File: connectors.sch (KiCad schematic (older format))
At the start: 43 parts, among them J11 20021121-00010C4LF, J12 70543-0001, J13 70543-0001, J14 70543-0001, J15 70543-0001, J16 70543-0001, J17 70543-0001, J18 70543-0001, J19 70543-0001, J20 70543-0003, J21 70543-0002, J22 70543-0002, J23 70543-0002, J24 Conn_02x20_Odd_Even

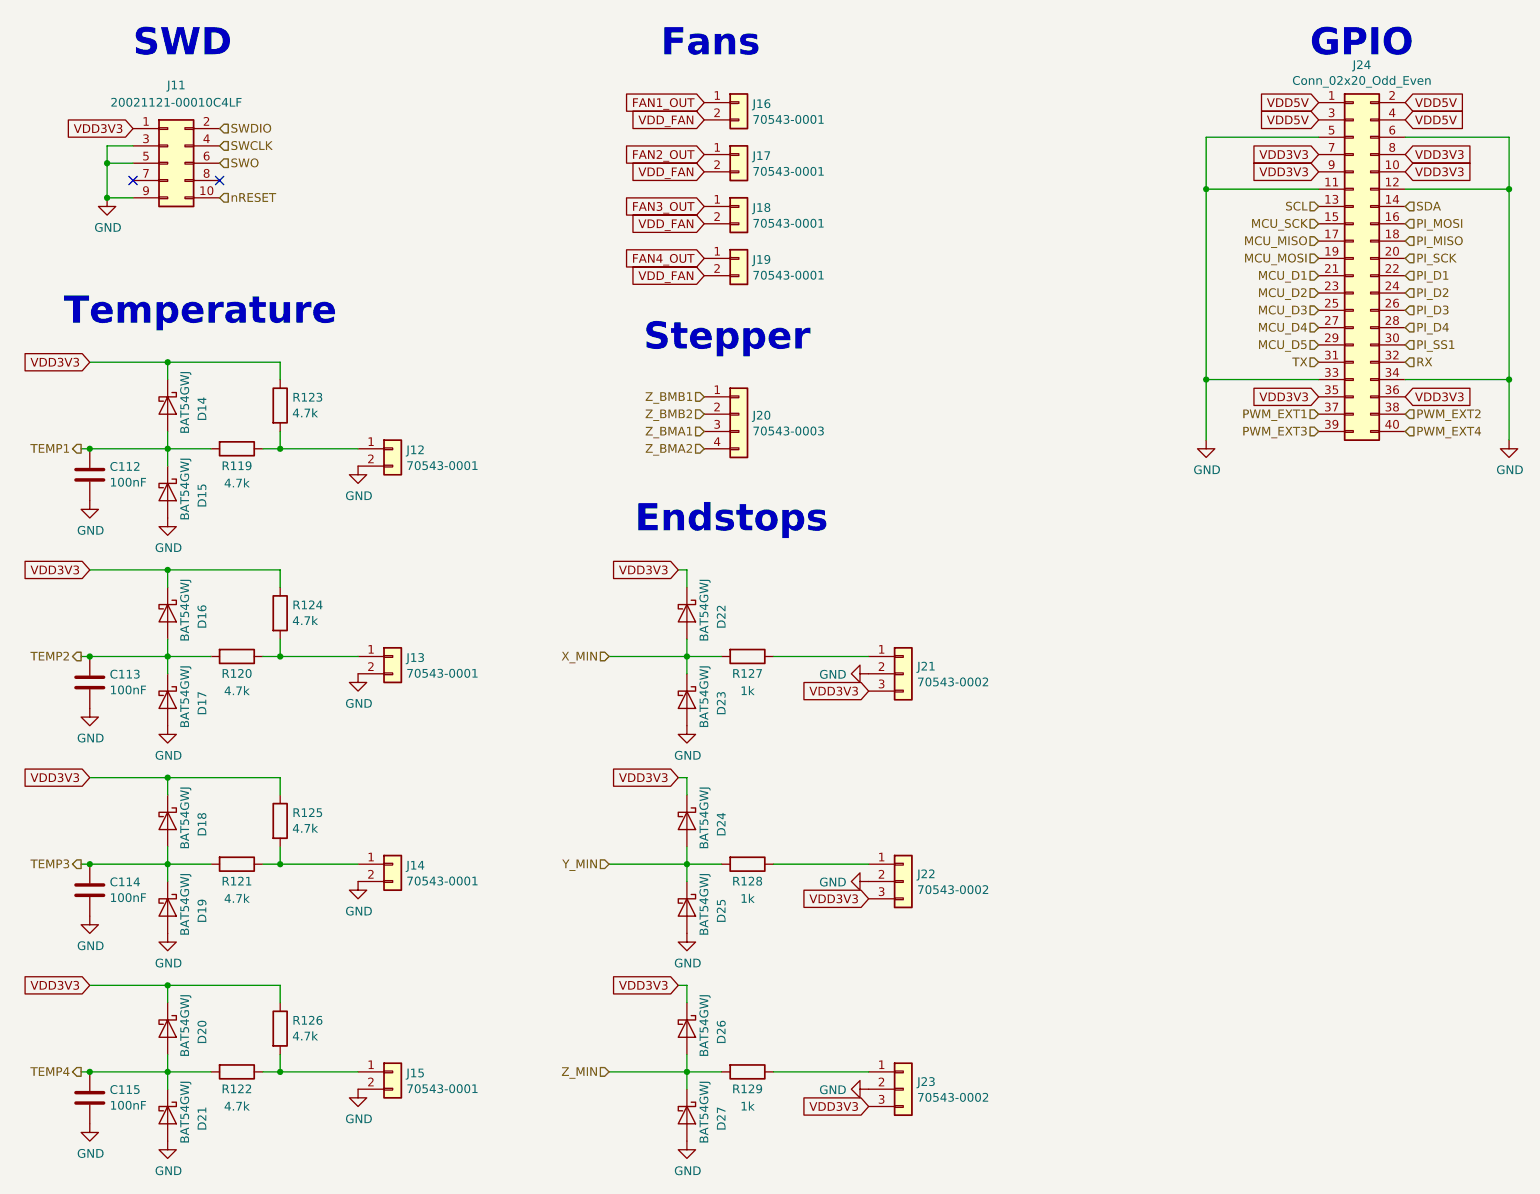
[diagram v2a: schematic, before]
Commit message: Add PU for SD_DETECT_PIN
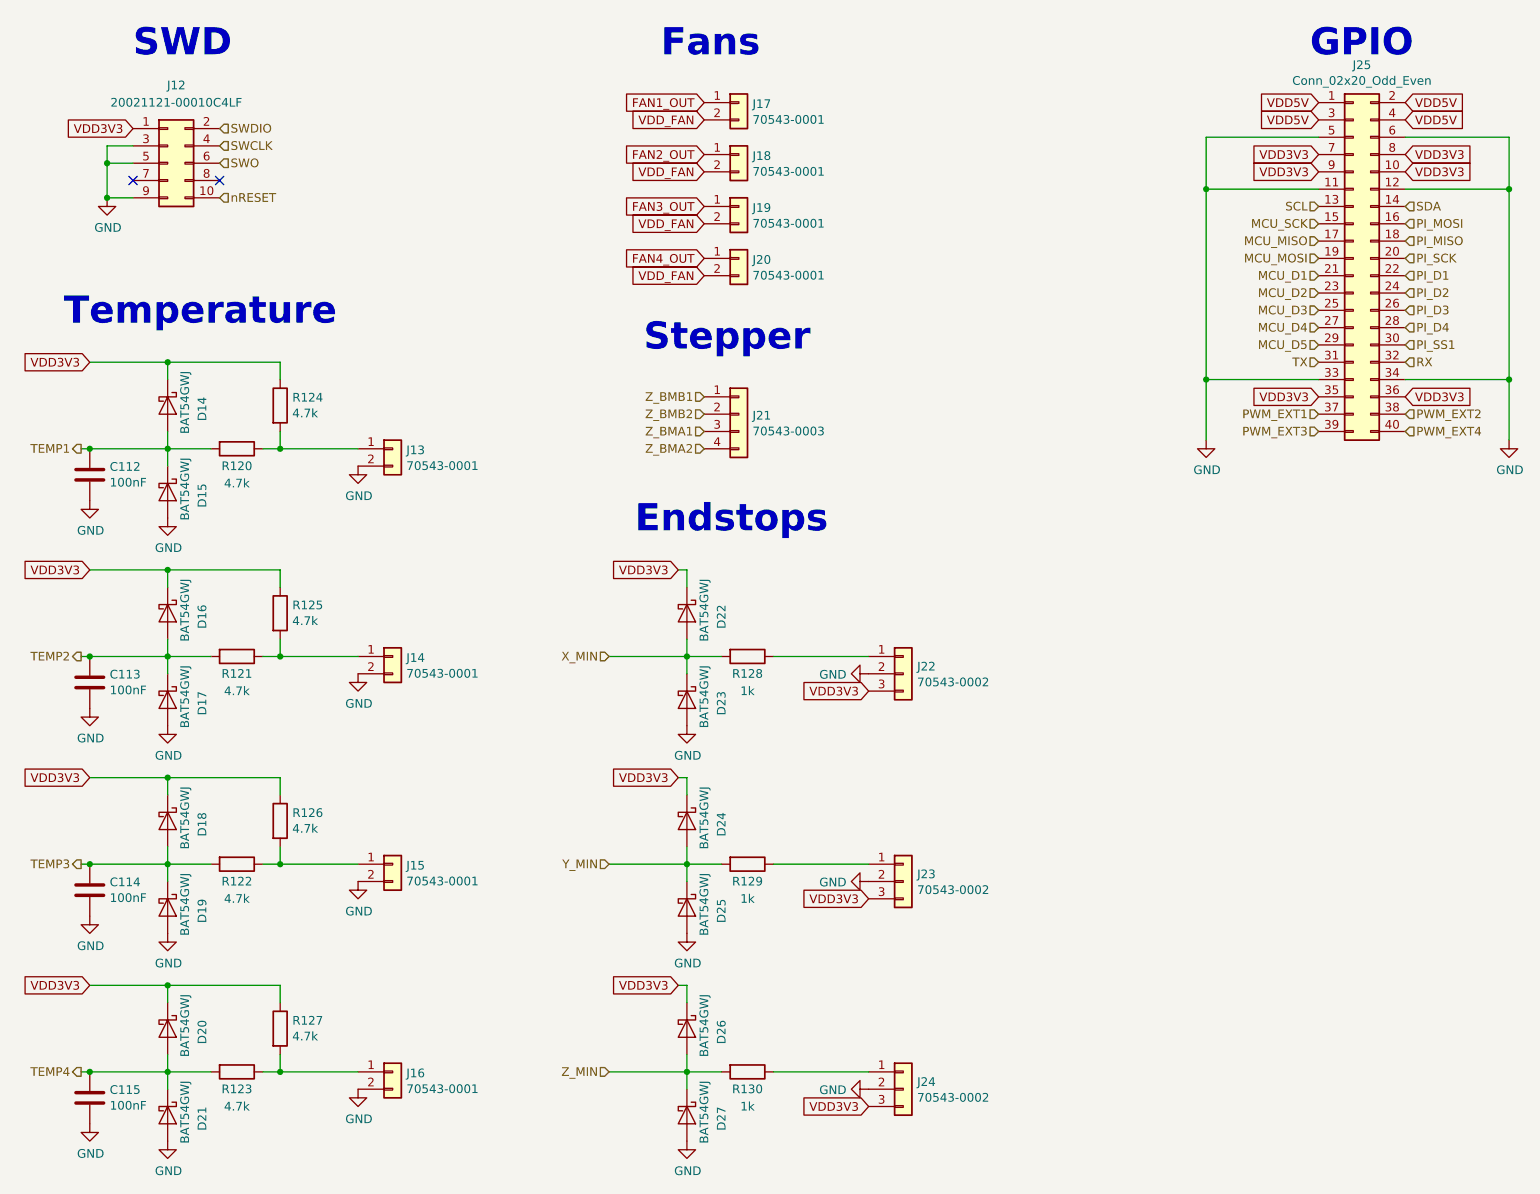
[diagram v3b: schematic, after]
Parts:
- renumbered J11 to J12, J12 to J13, J13 to J14, J14 to J15, J15 to J16, J16 to J17, J17 to J18, J18 to J19, J19 to J20, J20 to J21, J21 to J22, J22 to J23, J23 to J24, J24 to J25, R119 to R120, R120 to R121, R121 to R122, R122 to R123, R123 to R124, R124 to R125, R125 to R126, R126 to R127, R127 to R128, R128 to R129, R129 to R130
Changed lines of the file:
@@
 TEMP1
 $Comp
-L Device:R R119
+L Device:R R120
 U 1 1 5B1719A1
 P 1900 3300
-F 0 "R119" V 2000 3300 50  0000 C CNN
+F 0 "R120" V 2000 3300 50  0000 C CNN
 F 1 "4.7k" V 2100 3300 50  0000 C CNN
 F 2 "Resistor_SMD:R_0603_1608Metric" V 1830 3300 50  0001 C CNN
@@
 $EndComp
 $Comp
-L Device:R R123
+L Device:R R124
 U 1 1 5B1719A8
 P 2150 3050
-F 0 "R123" H 2220 3096 50  0000 L CNN
+F 0 "R124" H 2220 3096 50  0000 L CNN
 F 1 "4.7k" H 2220 3005 50  0000 L CNN
 F 2 "Resistor_SMD:R_0603_1608Metric" V 2080 3050 50  0001 C CNN
@@
 	2150 3300 2150 3200
 $Comp
-L Connector_Generic:Conn_01x02 J12
+L Connector_Generic:Conn_01x02 J13
 U 1 1 5B1719C1
 P 2800 3300
-F 0 "J12" H 2879 3292 50  0000 L CNN
+F 0 "J13" H 2879 3292 50  0000 L CNN
 F 1 "70543-0001" H 2879 3201 50  0000 L CNN
 F 2 "heteromycin:70543-0001" H 2800 3300 50  0001 C CNN
@@
 $EndComp
 $Comp
-L Connector_Generic:Conn_02x05_Odd_Even J11
+L Connector_Generic:Conn_02x05_Odd_Even J12
 U 1 1 5B17C4BC
 P 1500 1650
-F 0 "J11" H 1550 2100 50  0000 C CNN
+F 0 "J12" H 1550 2100 50  0000 C CNN
 F 1 "20021121-00010C4LF" H 1550 2000 50  0000 C CNN
 F 2 "Connector_PinHeader_1.27mm:PinHeader_2x05_P1.27mm_Vertical_SMD" H 1500 1650 50  0001 C CNN
@@
 NoConn ~ 1800 1750
 $Comp
-L Connector_Generic:Conn_01x04 J20
+L Connector_Generic:Conn_01x04 J21
 U 1 1 5AFD917C
 P 4800 3100
-F 0 "J20" H 4879 3092 50  0000 L CNN
+F 0 "J21" H 4879 3092 50  0000 L CNN
 F 1 "70543-0003" H 4879 3001 50  0000 L CNN
 F 2 "heteromycin:70543-0003" H 4800 3100 50  0001 C CNN
@@
 VDD_FAN
 $Comp
-L Device:R R127
+L Device:R R128
 U 1 1 5B40FD8A
 P 4850 4500
-F 0 "R127" V 4950 4500 50  0000 C CNN
+F 0 "R128" V 4950 4500 50  0000 C CNN
 F 1 "1k" V 5050 4500 50  0000 C CNN
 F 2 "Resistor_SMD:R_0603_1608Metric" V 4780 4500 50  0001 C CNN
@@
 	4500 4500 4700 4500
 $Comp
-L Device:R R128
+L Device:R R129
 U 1 1 5B453619
 P 4850 5700
-F 0 "R128" V 4950 5700 50  0000 C CNN
+F 0 "R129" V 4950 5700 50  0000 C CNN
 F 1 "1k" V 5050 5700 50  0000 C CNN
 F 2 "Resistor_SMD:R_0603_1608Metric" V 4780 5700 50  0001 C CNN
@@
 	4500 5700 4700 5700
 $Comp
-L Device:R R129
+L Device:R R130
 U 1 1 5B45771E
 P 4850 6900
-F 0 "R129" V 4950 6900 50  0000 C CNN
+F 0 "R130" V 4950 6900 50  0000 C CNN
 F 1 "1k" V 5050 6900 50  0000 C CNN
 F 2 "Resistor_SMD:R_0603_1608Metric" V 4780 6900 50  0001 C CNN
@@
 Connection ~ 2150 3300
 $Comp
-L Device:R R120
+L Device:R R121
 U 1 1 5B5657F4
 P 1900 4500
-F 0 "R120" V 2000 4500 50  0000 C CNN
+F 0 "R121" V 2000 4500 50  0000 C CNN
 F 1 "4.7k" V 2100 4500 50  0000 C CNN
 F 2 "Resistor_SMD:R_0603_1608Metric" V 1830 4500 50  0001 C CNN
@@
 $EndComp
 $Comp
-L Device:R R124
+L Device:R R125
 U 1 1 5B5657FB
 P 2150 4250
-F 0 "R124" H 2220 4296 50  0000 L CNN
+F 0 "R125" H 2220 4296 50  0000 L CNN
 F 1 "4.7k" H 2220 4205 50  0000 L CNN
 F 2 "Resistor_SMD:R_0603_1608Metric" V 2080 4250 50  0001 C CNN
@@
 Connection ~ 2150 4500
 $Comp
-L Device:R R121
+L Device:R R122
 U 1 1 5B57C5BA
 P 1900 5700
-F 0 "R121" V 2000 5700 50  0000 C CNN
+F 0 "R122" V 2000 5700 50  0000 C CNN
 F 1 "4.7k" V 2100 5700 50  0000 C CNN
 F 2 "Resistor_SMD:R_0603_1608Metric" V 1830 5700 50  0001 C CNN
@@
 $EndComp
 $Comp
-L Device:R R125
+L Device:R R126
 U 1 1 5B57C5C1
 P 2150 5450
-F 0 "R125" H 2220 5496 50  0000 L CNN
+F 0 "R126" H 2220 5496 50  0000 L CNN
 F 1 "4.7k" H 2220 5405 50  0000 L CNN
 F 2 "Resistor_SMD:R_0603_1608Metric" V 2080 5450 50  0001 C CNN
@@
 $EndComp
 $Comp
-L Device:R R122
+L Device:R R123
 U 1 1 5BC983A7
 P 1900 6900
-F 0 "R122" V 2000 6900 50  0000 C CNN
+F 0 "R123" V 2000 6900 50  0000 C CNN
 F 1 "4.7k" V 2100 6900 50  0000 C CNN
 F 2 "Resistor_SMD:R_0603_1608Metric" V 1830 6900 50  0001 C CNN
@@
 $EndComp
 $Comp
-L Device:R R126
+L Device:R R127
 U 1 1 5BC983AE
 P 2150 6650
-F 0 "R126" H 2220 6696 50  0000 L CNN
+F 0 "R127" H 2220 6696 50  0000 L CNN
 F 1 "4.7k" H 2220 6605 50  0000 L CNN
 F 2 "Resistor_SMD:R_0603_1608Metric" V 2080 6650 50  0001 C CNN
@@
 	2150 6900 2600 6900
 $Comp
-L Connector_Generic:Conn_01x02 J16
+L Connector_Generic:Conn_01x02 J17
 U 1 1 5BCF44AA
 P 4800 1300
-F 0 "J16" H 4879 1292 50  0000 L CNN
+F 0 "J17" H 4879 1292 50  0000 L CNN
 F 1 "70543-0001" H 4879 1201 50  0000 L CNN
 F 2 "heteromycin:70543-0001" H 4800 1300 50  0001 C CNN
@@
 GPIO
 $Comp
-L Connector_Generic:Conn_02x20_Odd_Even J24
+L Connector_Generic:Conn_02x20_Odd_Even J25
 U 1 1 5BD1EAFC
 P 8350 2200
-F 0 "J24" H 8400 3317 50  0000 C CNN
+F 0 "J25" H 8400 3317 50  0000 C CNN
 F 1 "Conn_02x20_Odd_Even" H 8400 3226 50  0000 C CNN
 F 2 "Connector_PinHeader_2.54mm:PinHeader_2x20_P2.54mm_Vertical_SMD" H 8350 2200 50  0001 C CNN
@@
 $EndComp
 $Comp
-L Connector_Generic:Conn_01x02 J17
+L Connector_Generic:Conn_01x02 J18
 U 1 1 5BC6B4B4
 P 4800 1600
-F 0 "J17" H 4879 1592 50  0000 L CNN
+F 0 "J18" H 4879 1592 50  0000 L CNN
 F 1 "70543-0001" H 4879 1501 50  0000 L CNN
 F 2 "heteromycin:70543-0001" H 4800 1600 50  0001 C CNN
@@
 $EndComp
 $Comp
-L Connector_Generic:Conn_01x02 J18
+L Connector_Generic:Conn_01x02 J19
 U 1 1 5BC6CFF2
 P 4800 1900
-F 0 "J18" H 4879 1892 50  0000 L CNN
+F 0 "J19" H 4879 1892 50  0000 L CNN
 F 1 "70543-0001" H 4879 1801 50  0000 L CNN
 F 2 "heteromycin:70543-0001" H 4800 1900 50  0001 C CNN
@@
 $EndComp
 $Comp
-L Connector_Generic:Conn_01x02 J19
+L Connector_Generic:Conn_01x02 J20
 U 1 1 5BC6EB34
 P 4800 2200
-F 0 "J19" H 4879 2192 50  0000 L CNN
+F 0 "J20" H 4879 2192 50  0000 L CNN
 F 1 "70543-0001" H 4879 2101 50  0000 L CNN
 F 2 "heteromycin:70543-0001" H 4800 2200 50  0001 C CNN
@@
 $EndComp
 $Comp
-L Connector_Generic:Conn_01x02 J13
+L Connector_Generic:Conn_01x02 J14
 U 1 1 5BC787B3
 P 2800 4500
-F 0 "J13" H 2879 4492 50  0000 L CNN
+F 0 "J14" H 2879 4492 50  0000 L CNN
 F 1 "70543-0001" H 2879 4401 50  0000 L CNN
 F 2 "heteromycin:70543-0001" H 2800 4500 50  0001 C CNN
@@
 $EndComp
 $Comp
-L Connector_Generic:Conn_01x02 J14
+L Connector_Generic:Conn_01x02 J15
 U 1 1 5BC7A30D
 P 2800 5700
-F 0 "J14" H 2879 5692 50  0000 L CNN
+F 0 "J15" H 2879 5692 50  0000 L CNN
 F 1 "70543-0001" H 2879 5601 50  0000 L CNN
 F 2 "heteromycin:70543-0001" H 2800 5700 50  0001 C CNN
@@
 $EndComp
 $Comp
-L Connector_Generic:Conn_01x02 J15
+L Connector_Generic:Conn_01x02 J16
 U 1 1 5BC7BE61
 P 2800 6900
-F 0 "J15" H 2879 6892 50  0000 L CNN
+F 0 "J16" H 2879 6892 50  0000 L CNN
 F 1 "70543-0001" H 2879 6801 50  0000 L CNN
 F 2 "heteromycin:70543-0001" H 2800 6900 50  0001 C CNN
@@
 FAN4_OUT
 $Comp
-L Connector_Generic:Conn_01x03 J21
+L Connector_Generic:Conn_01x03 J22
 U 1 1 5BCA3C01
 P 5750 4600
-F 0 "J21" H 5830 4642 50  0000 L CNN
+F 0 "J22" H 5830 4642 50  0000 L CNN
 F 1 "70543-0002" H 5830 4551 50  0000 L CNN
 F 2 "heteromycin:70543-0002" H 5750 4600 50  0001 C CNN
@@
 $EndComp
 $Comp
-L Connector_Generic:Conn_01x03 J22
+L Connector_Generic:Conn_01x03 J23
 U 1 1 5BCAFD14
 P 5750 5800
-F 0 "J22" H 5830 5842 50  0000 L CNN
+F 0 "J23" H 5830 5842 50  0000 L CNN
 F 1 "70543-0002" H 5830 5751 50  0000 L CNN
 F 2 "heteromycin:70543-0002" H 5750 5800 50  0001 C CNN
@@
 $EndComp
 $Comp
-L Connector_Generic:Conn_01x03 J23
+L Connector_Generic:Conn_01x03 J24
 U 1 1 5BCB490A
 P 5750 7000
-F 0 "J23" H 5830 7042 50  0000 L CNN
+F 0 "J24" H 5830 7042 50  0000 L CNN
 F 1 "70543-0002" H 5830 6951 50  0000 L CNN
 F 2 "heteromycin:70543-0002" H 5750 7000 50  0001 C CNN

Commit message: Further Improved Readability - Rotated labels
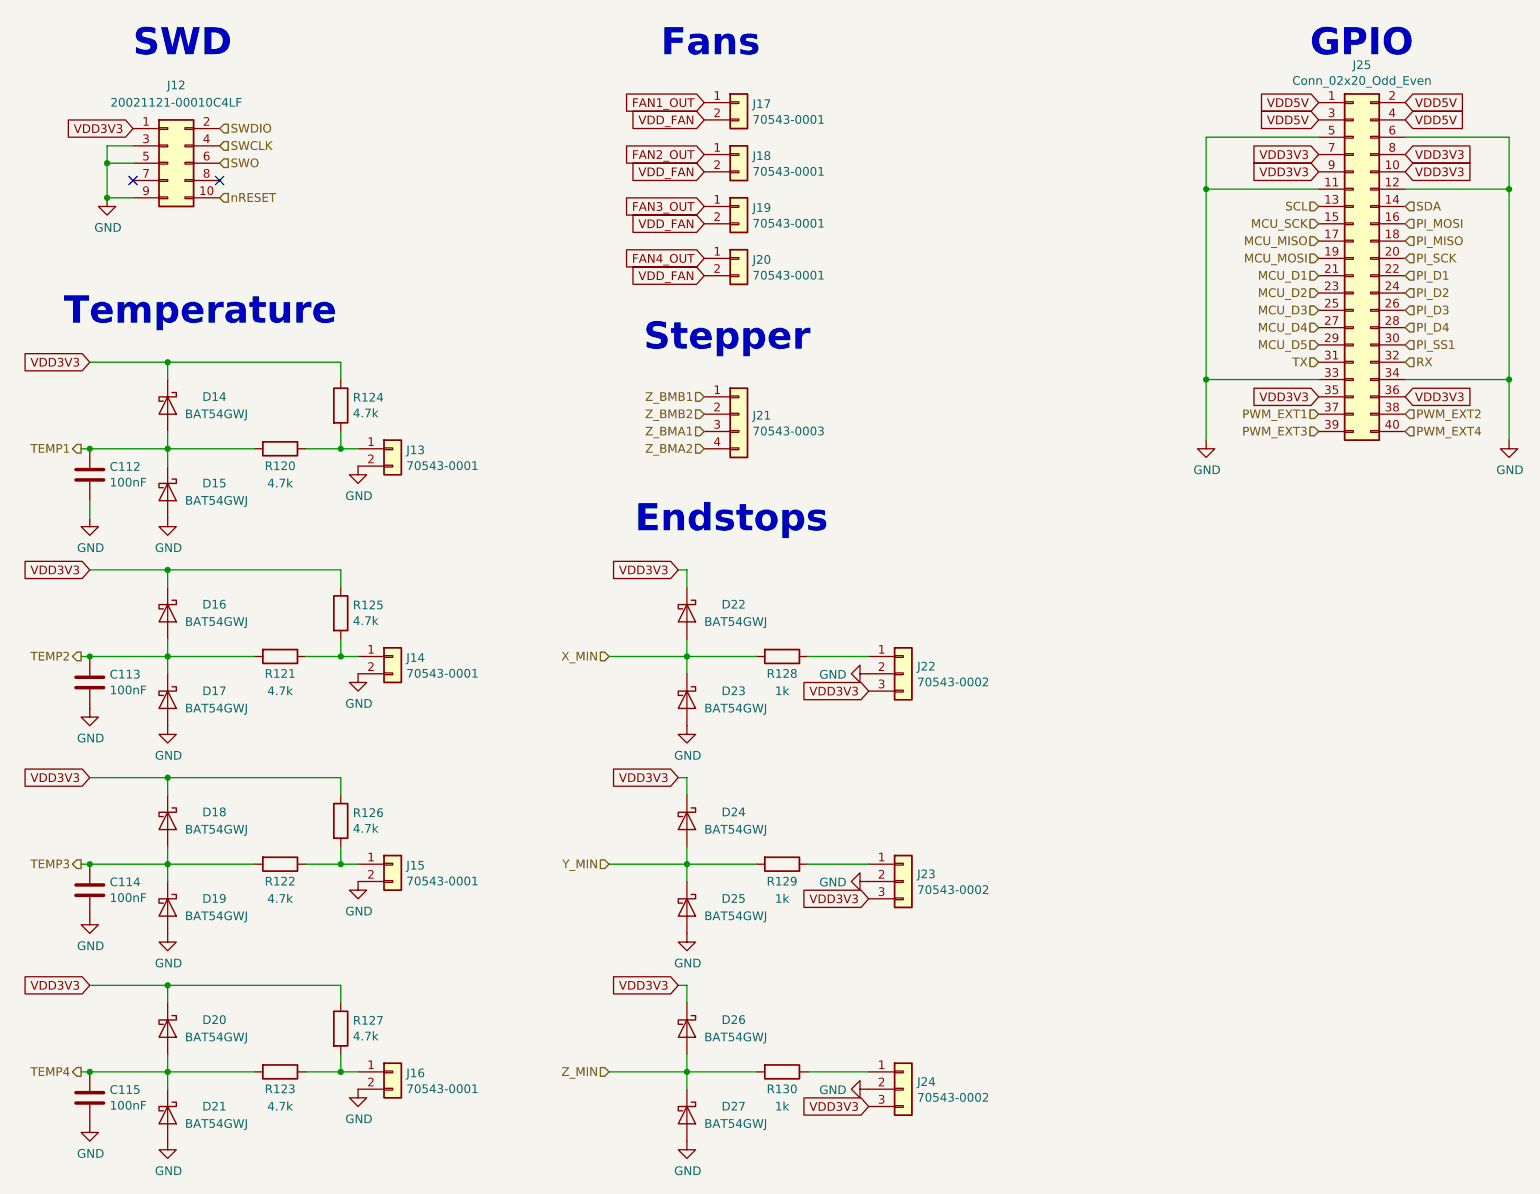
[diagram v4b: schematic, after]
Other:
- moved on the sheet: R120, R121, R122, R123, R124, R125, R126, R127, R128, R129, R130
